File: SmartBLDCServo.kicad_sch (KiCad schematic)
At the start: 20 parts, among them J1 TTL Half Duplex, J2 AS5600, J3 Stepper, U1 ESP32-C3-SuperMini, U2 TMC2209_SILENTSTEPSTICK, U3 MP1584EN_8Pin_Module, U4 BOB-12009

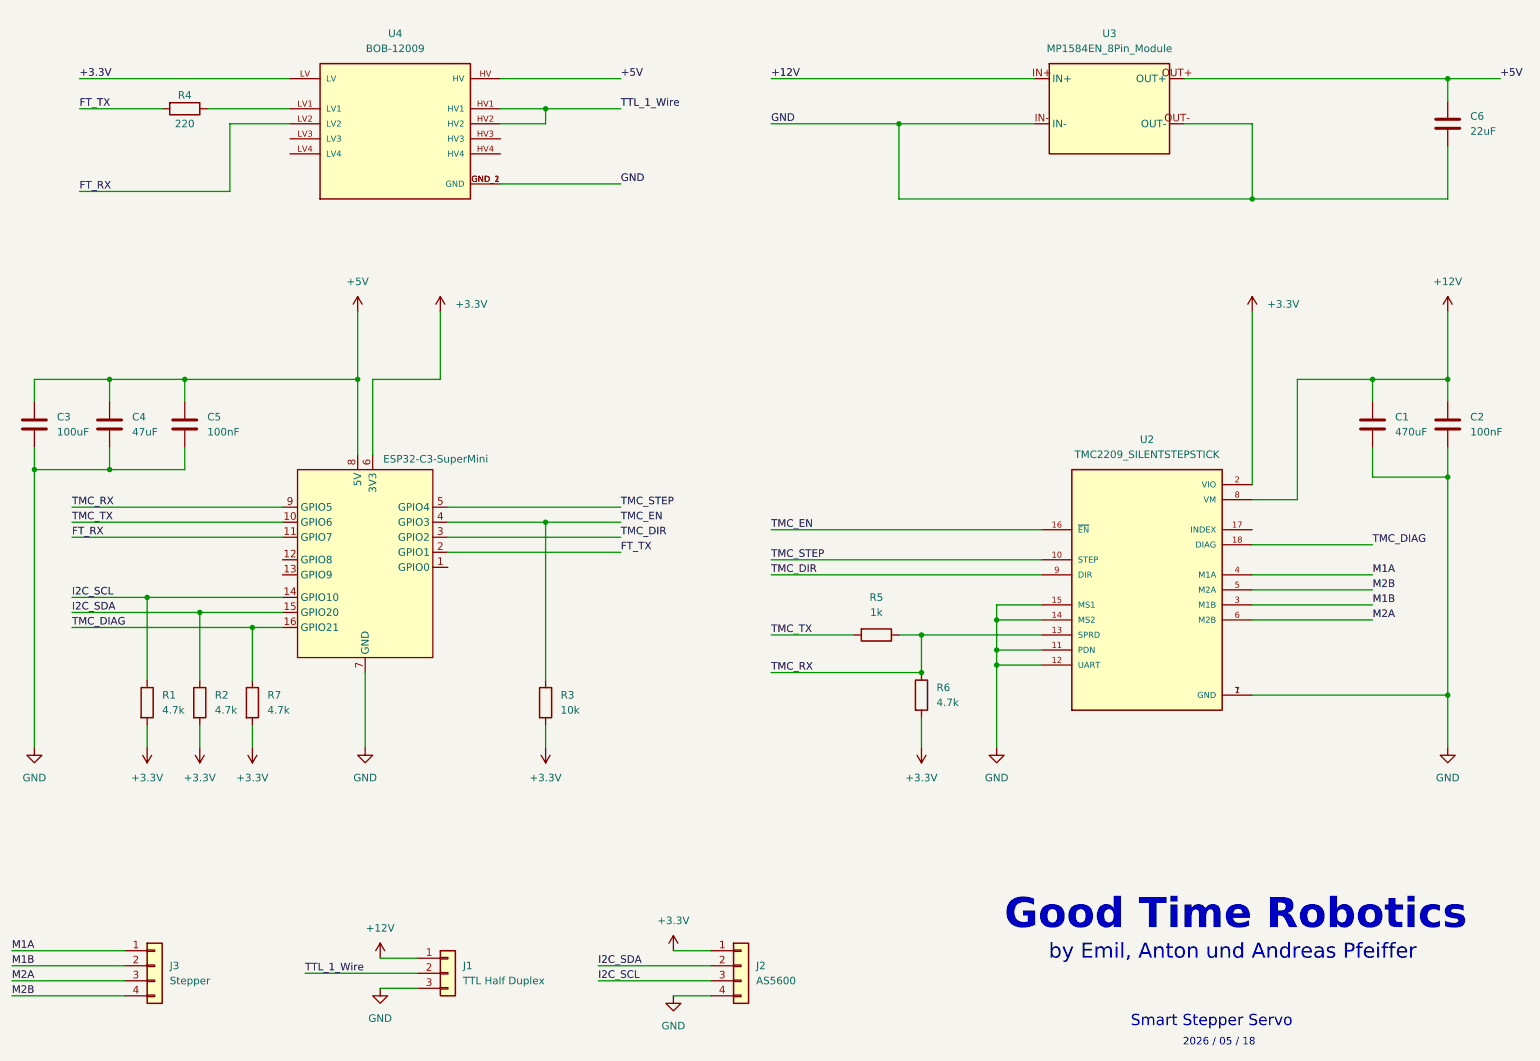
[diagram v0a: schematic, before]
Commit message: Add OpenLoopTest firmware, Web GUI and update project README
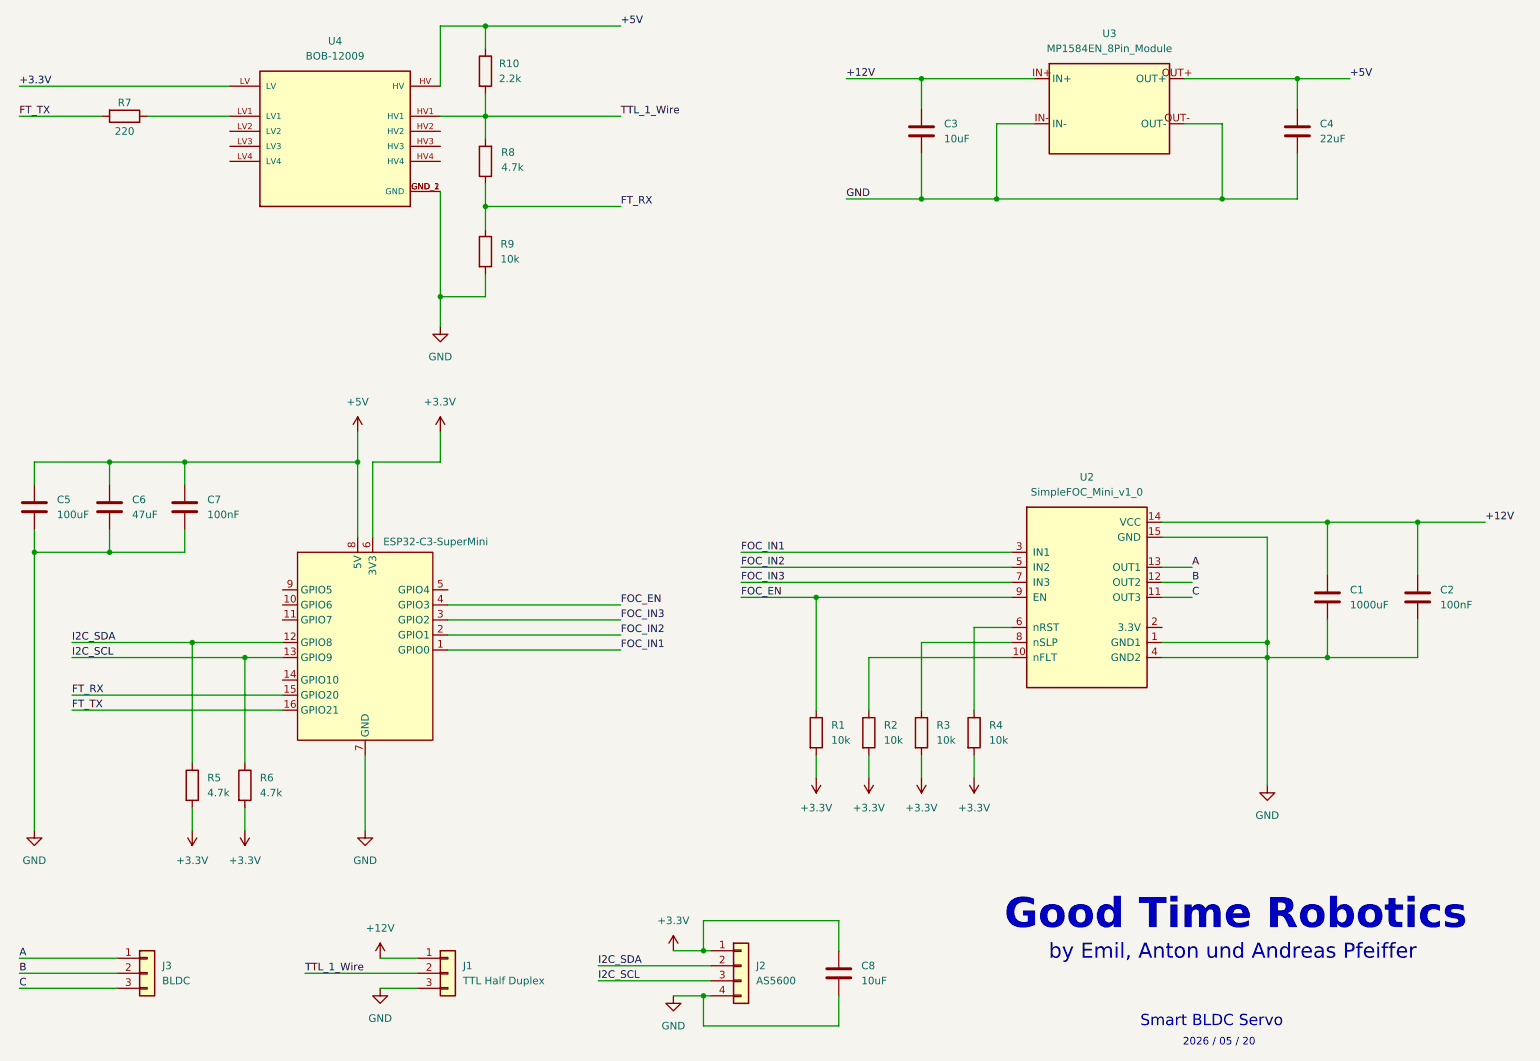
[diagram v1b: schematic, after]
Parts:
- removed J3: Stepper, JST_XH_B4B-XH-A_1x04_P2.50mm_Vertical, symbol Connector_Generic:Conn_01x04
- removed R5: 1k, Resistor_THT:R_Axial_DIN0207_L6.3mm_D2.5mm_P7.62mm_Horizontal, symbol Device:R
- removed R6, R7: 4.7k, Resistor_THT:R_Axial_DIN0207_L6.3mm_D2.5mm_P7.62mm_Horizontal, symbol Device:R
- removed U2: TMC2209_SILENTSTEPSTICK, TMC2209_SILENTSTEPSTICK:MODULE_TMC2209_SILENTSTEPSTICK, symbol TMC2209_SILENTSTEPSTICK:TMC2209_SILENTSTEPSTICK
- added C3: 10uF, Capacitor_THT:C_Disc_D3.8mm_W2.6mm_P2.50mm, symbol Device:C
- added C8: 10uF, Capacitor_THT:CP_Radial_D6.3mm_P2.50mm, symbol Device:C
- added J3: BLDC, JST_XH_B3B-XH-A_1x03_P2.50mm_Vertical, symbol Connector_Generic:Conn_01x03
- added R1, R2, R4, R9: 10k, Resistor_THT:R_Axial_DIN0207_L6.3mm_D2.5mm_P7.62mm_Horizontal, symbol Device:R
- added R10: 2.2k, Resistor_THT:R_Axial_DIN0207_L6.3mm_D2.5mm_P7.62mm_Horizontal, symbol Device:R
- added R8: 4.7k, Resistor_THT:R_Axial_DIN0207_L6.3mm_D2.5mm_P7.62mm_Horizontal, symbol Device:R
- added U2: SimpleFOC_Mini_v1_0, simplefoc_mini:SimpleFOC_Mini_v1_0, symbol simplefoc_mini:SimpleFOC_Mini_v1_0
- C1: value 470uF -> 1000uF
- renumbered C6 to C4, C3 to C5, C4 to C6, C5 to C7, R1 to R5, R2 to R6, R4 to R7
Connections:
- net TMC_DIAG is gone; now on net FT_TX: U1.16 (GPIO21)
- net +12V: now also C1.2, C2.2, C3.1, U2.14 (VCC); no longer C1.1, C2.1
- net +3.3V: now also C8.2, R1.2, R2.2, R4.2
- net +5V: now also R10.1
- net FT_RX: now also U1.15 (GPIO20), R8.1, R9.1; no longer U1.11 (GPIO7), U4.LV2
- net FT_TX: no longer U1.2 (GPIO1)
- net GND: now also C1.1, C2.1, C3.2, C8.1, R9.2, U2.1 (GND1), U2.15 (GND), U2.4 (GND2); no longer C1.2, C2.2
- net I2C_SCL: now also R6.1, U1.13 (GPIO9); no longer R5.1, U1.14 (GPIO10)
- net I2C_SDA: now also R5.1, U1.12 (GPIO8); no longer R6.1, U1.15 (GPIO20)
- net TTL_1_Wire: now also R10.2, R8.2; no longer U4.HV2
- net FOC_IN1: now reaches U1.1 (GPIO0)
- net FOC_IN1: now also U2.3 (IN1)
- net TMC_DIR renamed FOC_IN3
- net FOC_IN3: now also U2.7 (IN3)
- net TMC_EN: no longer names the net of R3.1
- net TMC_EN: now also U2.8 (nSLP); no longer U1.4 (GPIO3)
- net TMC_RX: no longer names the net of U1.9 (GPIO5)
- net TMC_STEP: no longer names the net of U1.5 (GPIO4)
- net TMC_TX: no longer names the net of U1.10 (GPIO6)
- new net: R2.1, U2.10 (nFLT)
- new net: R4.1, U2.6 (nRST)
- new net A: J3.1 (Pin_1), U2.13 (OUT1)
- new net B: J3.2 (Pin_2), U2.12 (OUT2)
- new net C: J3.3 (Pin_3), U2.11 (OUT3)
- new net FOC_EN: R1.1, U1.4 (GPIO3), U2.9 (EN)
- new net FOC_IN2: U1.2 (GPIO1), U2.5 (IN2)
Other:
- note added: "2026 / 05 / 20"
- note added: "Smart BLDC Servo"
- note removed: "2026 / 05 / 18"
- note removed: "Smart Stepper Servo"
- moved on the sheet: C4, C5, C6, C7, R5, R6, R7, U4

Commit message: Update KiCad schematic with final TVS diode, capacitor, and FOC_nFLT label additions
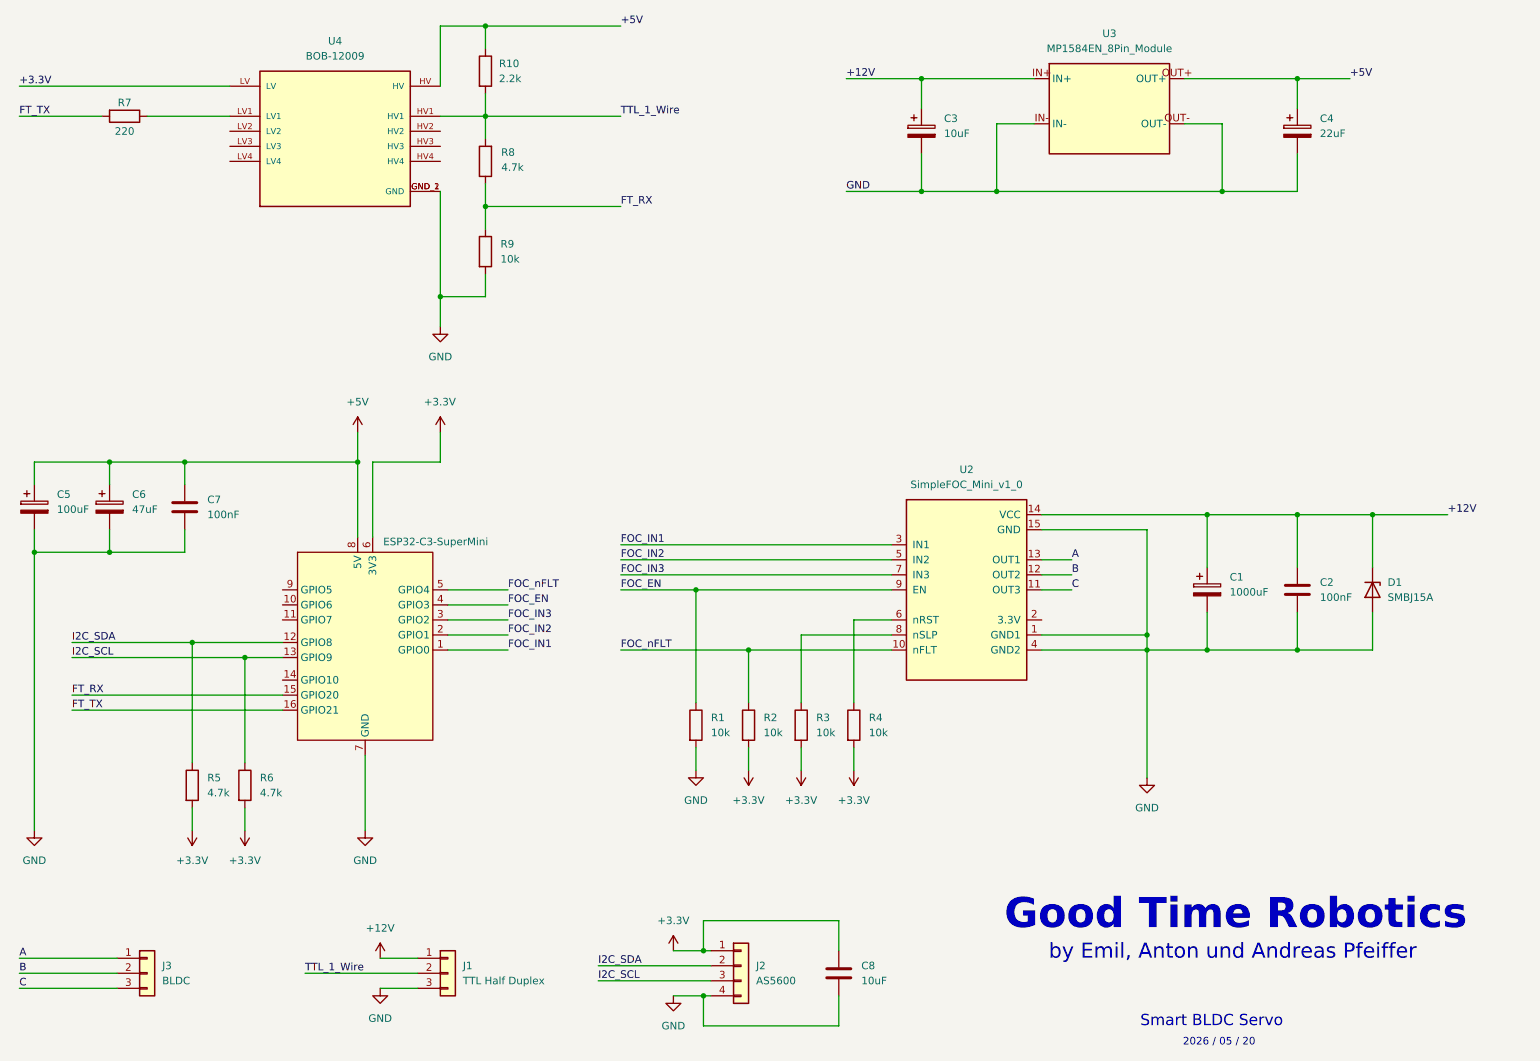
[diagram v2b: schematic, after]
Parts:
- removed C1: 1000uF, Capacitor_THT:CP_Radial_D6.3mm_P2.50mm, symbol Device:C
- removed C3: 10uF, Capacitor_THT:C_Disc_D3.8mm_W2.6mm_P2.50mm, symbol Device:C
- removed C4: 22uF, Capacitor_THT:C_Disc_D3.8mm_W2.6mm_P2.50mm, symbol Device:C
- removed C5: 100uF, Capacitor_THT:CP_Radial_D6.3mm_P2.50mm, symbol Device:C
- removed C6: 47uF, Capacitor_THT:CP_Radial_D6.3mm_P2.50mm, symbol Device:C
- added C1: 1000uF, symbol Device:C_Polarized
- added C3: 10uF, symbol Device:C_Polarized
- added C4: 22uF, symbol Device:C_Polarized
- added C5: 100uF, symbol Device:C_Polarized
- added C6: 47uF, symbol Device:C_Polarized
- added D1: SMBJ15A, Diode_SMD:D_SMB, symbol Device:D_Zener
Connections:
- net +12V: now also C1.1, C3.1, D1.1 (K)
- net +3.3V: no longer R1.2
- net +5V: now also C4.1, C5.1, C6.1
- net GND: now also R1.2, C1.2, C3.2, C4.2, C5.2, C6.2, D1.2 (A)
- net FOC_nFLT: now reaches R2.1, U2.10 (nFLT)
- net FOC_nFLT: now also U1.5 (GPIO4)
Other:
- moved on the sheet: C2, R1, R2, R3, R4, U2

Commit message: Update KiCad PCB and schematic: Fix footprint UUIDs, add SimpleFOC and MP1584EN footprints
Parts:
- J1, J3: footprint JST_XH_B3B-XH-A_1x03_P2.50mm_Vertical -> Connector_JST:JST_XH_B3B-XH-A_1x03_P2.50mm_Vertical
- J2: footprint JST_XH_B4B-XH-A_1x04_P2.50mm_Vertical -> Connector_JST:JST_XH_B4B-XH-A_1x04_P2.50mm_Vertical
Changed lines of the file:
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@@
 			)
 		)
-		(property "Footprint" "JST_XH_B3B-XH-A_1x03_P2.50mm_Vertical"
+		(property "Footprint" "Connector_JST:JST_XH_B3B-XH-A_1x03_P2.50mm_Vertical"
 			(at 46.99 181.61 0)
 			(hide yes)
@@
 			)
 		)
-		(property "Footprint" "JST_XH_B3B-XH-A_1x03_P2.50mm_Vertical"
+		(property "Footprint" "Connector_JST:JST_XH_B3B-XH-A_1x03_P2.50mm_Vertical"
 			(at 97.79 181.61 0)
 			(hide yes)
@@
 			)
 		)
-		(property "Footprint" "JST_XH_B4B-XH-A_1x04_P2.50mm_Vertical"
+		(property "Footprint" "Connector_JST:JST_XH_B4B-XH-A_1x04_P2.50mm_Vertical"
 			(at 147.32 180.34 0)
 			(hide yes)
